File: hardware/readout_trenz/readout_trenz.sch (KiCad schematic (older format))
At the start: 1 part

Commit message: Finishing Readout Schematic
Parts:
- gave numbers to parts that had none: 1
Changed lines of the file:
@@
 B2_[0..31]
 Wire Wire Line
-	12850 5050 12800 5050
-Connection ~ 12850 5050
+	13100 5200 13050 5200
+Connection ~ 13100 5200
 Wire Wire Line
-	12850 5050 12850 5200
+	13100 5200 13100 5350
 Wire Wire Line
-	12800 4950 12850 4950
+	13050 5100 13100 5100
 Wire Wire Line
-	12850 4950 12850 5050
-Text Label 11750 5050 0    50   ~ 0
+	13100 5100 13100 5200
+Text Label 12000 5200 0    50   ~ 0
 LVDS_GPIO_n2
 Wire Wire Line
-	12300 4950 11750 4950
+	12550 5100 12000 5100
 Wire Wire Line
-	11750 5050 12300 5050
+	12000 5200 12550 5200
 $Comp
-L power:GNDD #PWR?
+L power:GNDD #PWR01
 U 1 1 60B06DB5
-P 12850 5200
-F 0 "#PWR?" H 12850 4950 50  0001 C CNN
-F 1 "GNDD-power" H 12854 5045 50  0000 C CNN
-F 2 "" H 12850 5200 50  0001 C CNN
-F 3 "" H 12850 5200 50  0001 C CNN
-	1    12850 5200
+P 13100 5350
+F 0 "#PWR01" H 13100 5100 50  0001 C CNN
+F 1 "GNDD-power" H 13104 5195 50  0000 C CNN
+F 2 "" H 13100 5350 50  0001 C CNN
+F 3 "" H 13100 5350 50  0001 C CNN
+	1    13100 5350
 	1    0    0    -1
 $EndComp
-Connection ~ 12850 4950
+Connection ~ 13100 5100
 $Comp
-L Connector_Generic:Conn_02x12_Counter_Clockwise J?
+L Connector_Generic:Conn_02x12_Counter_Clockwise J1
 U 1 1 60B1DFBC
-P 12500 4450
-F 0 "J?" H 12550 5167 50  0000 C CNN
-F 1 "Conn_02x12_Counter_Clockwise" H 12550 5076 50  0000 C CNN
-F 2 "" H 12500 4450 50  0001 C CNN
-F 3 "~" H 12500 4450 50  0001 C CNN
-	1    12500 4450
+P 12750 4600
+F 0 "J1" H 12800 5317 50  0000 C CNN
+F 1 "Conn_02x12_Counter_Clockwise" H 12800 5226 50  0000 C CNN
+F 2 "" H 12750 4600 50  0001 C CNN
+F 3 "~" H 12750 4600 50  0001 C CNN
+	1    12750 4600
 	1    0    0    -1
 $EndComp
 Wire Wire Line
-	12300 4450 11850 4450
+	12550 4600 12100 4600
 Wire Wire Line
-	11850 4350 12300 4350
-Text Label 11850 4450 0    50   ~ 0
+	12100 4500 12550 4500
+Text Label 12100 4600 0    50   ~ 0
 3v3_GPIO2
-Text Label 11850 4350 0    50   ~ 0
+Text Label 12100 4500 0    50   ~ 0
 3v3_GPIO1
 Wire Wire Line
-	12300 4650 11850 4650
+	12550 4800 12100 4800
 Wire Wire Line
-	11850 4550 12300 4550
-Text Label 11850 4650 0    50   ~ 0
+	12100 4700 12550 4700
+Text Label 12100 4800 0    50   ~ 0
 3v3_GPIO4
-Text Label 11850 4550 0    50   ~ 0
+Text Label 12100 4700 0    50   ~ 0
 3v3_GPIO3
-Text Label 11750 4950 0    50   ~ 0
+Text Label 12000 5100 0    50   ~ 0
 LVDS_GPIO_p2
 Wire Wire Line
-	11750 4850 12300 4850
+	12000 5000 12550 5000
 Wire Wire Line
-	12300 4750 11750 4750
-Text Label 11750 4850 0    50   ~ 0
+	12550 4900 12000 4900
+Text Label 12000 5000 0    50   ~ 0
 LVDS_GPIO_n1
-Text Label 11750 4750 0    50   ~ 0
+Text Label 12000 4900 0    50   ~ 0
 LVDS_GPIO_p1
 Wire Wire Line
-	12300 4050 11850 4050
+	12550 4200 12100 4200
 Wire Wire Line
-	11850 3950 12300 3950
-Text Label 11850 4050 0    50   ~ 0
+	12100 4100 12550 4100
+Text Label 12100 4200 0    50   ~ 0
 1v8_GPIO2
-Text Label 11850 3950 0    50   ~ 0
+Text Label 12100 4100 0    50   ~ 0
 1v8_GPIO1
 Wire Wire Line
-	12300 4250 11850 4250
+	12550 4400 12100 4400
 Wire Wire Line
-	11850 4150 12300 4150
-Text Label 11850 4250 0    50   ~ 0
+	12100 4300 12550 4300
+Text Label 12100 4400 0    50   ~ 0
 1v8_GPIO4
-Text Label 11850 4150 0    50   ~ 0
+Text Label 12100 4300 0    50   ~ 0
 1v8_GPIO3
 Wire Wire Line
-	12850 4050 12850 4150
-Connection ~ 12850 4050
+	13100 4200 13100 4300
+Connection ~ 13100 4200
 Wire Wire Line
-	12850 4050 12800 4050
+	13100 4200 13050 4200
 Wire Wire Line
-	12850 4150 12850 4250
-Connection ~ 12850 4150
+	13100 4300 13100 4400
+Connection ~ 13100 4300
 Wire Wire Line
-	12800 4150 12850 4150
+	13050 4300 13100 4300
 Wire Wire Line
-	12850 4250 12850 4350
-Connection ~ 12850 4250
+	13100 4400 13100 4500
+Connection ~ 13100 4400
 Wire Wire Line
-	12850 4250 12800 4250
-Connection ~ 12850 4350
+	13100 4400 13050 4400
+Connection ~ 13100 4500
 Wire Wire Line
-	12850 3950 12850 4050
+	13100 4100 13100 4200
 Wire Wire Line
-	12800 3950 12850 3950
+	13050 4100 13100 4100
 Wire Wire Line
-	12850 4450 12850 4550
-Connection ~ 12850 4450
+	13100 4600 13100 4700
+Connection ~ 13100 4600
 Wire Wire Line
-	12850 4450 12800 4450
+	13100 4600 13050 4600
 Wire Wire Line
-	12850 4550 12850 4650
-Connection ~ 12850 4550
+	13100 4700 13100 4800
+Connection ~ 13100 4700
 Wire Wire Line
-	12800 4550 12850 4550
+	13050 4700 13100 4700
 Wire Wire Line
-	12850 4650 12850 4750
-Connection ~ 12850 4650
+	13100 4800 13100 4900
+Connection ~ 13100 4800
 Wire Wire Line
-	12850 4650 12800 4650
+	13100 4800 13050 4800
 Wire Wire Line
-	12850 4750 12850 4850
-Connection ~ 12850 4750
+	13100 4900 13100 5000
+Connection ~ 13100 4900
 Wire Wire Line
-	12800 4750 12850 4750
+	13050 4900 13100 4900
 Wire Wire Line
-	12850 4850 12850 4950
-Connection ~ 12850 4850
+	13100 5000 13100 5100
+Connection ~ 13100 5000
 Wire Wire Line
-	12850 4850 12800 4850
+	13100 5000 13050 5000
 Wire Wire Line
-	12850 4350 12850 4450
+	13100 4500 13100 4600
 Wire Wire Line
-	12800 4350 12850 4350
+	13050 4500 13100 4500
 Wire Wire Line
 	2500 6000 3500 6000

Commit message: _
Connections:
- wire segments 52 -> 44
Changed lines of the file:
@@
 	2500 6000 3500 6000
-Wire Bus Line
-	1300 6750 800  6750
-Entry Wire Line
-	1400 6150 1300 6250
-Entry Wire Line
-	1400 6250 1300 6350
-Entry Wire Line
-	1400 6350 1300 6450
-Entry Wire Line
-	1400 6450 1300 6550
-Entry Wire Line
-	800  6950 900  7050
-Entry Wire Line
-	800  7050 900  7150
-Entry Wire Line
-	800  7150 900  7250
-Entry Wire Line
-	800  7250 900  7350
-Wire Wire Line
-	1400 6150 1500 6150
-Wire Wire Line
-	1400 6250 1500 6250
-Wire Wire Line
-	1400 6350 1500 6350
-Wire Wire Line
-	1400 6450 1500 6450
-Wire Wire Line
-	900  7050 1000 7050
-Wire Wire Line
-	900  7150 1000 7150
-Wire Wire Line
-	900  7250 1000 7250
-Wire Wire Line
-	900  7350 1000 7350
 Wire Bus Line
 	4500 1500 5500 1500
@@
 F0 "POWER" 50
 F1 "POWER.sch" 50
-F2 "BIAS1" O L 1000 7050 50
-F3 "BIAS2" O L 1000 7150 50
-F4 "BIAS3" O L 1000 7250 50
-F5 "BIAS4" O L 1000 7350 50
-F6 "ENABLE" I R 6000 7050 50
+F2 "ENABLE" I R 6000 7050 50
+F3 "BIAS[1..4]" O L 1000 7050 50
 $EndSheet
 $Sheet
@@
 F1 "Backplane.sch" 50
 F2 "B2_[0..31]" O R 2500 4500 50
-F3 "BIAS1" I L 1500 6150 50
-F4 "BIAS2" I L 1500 6250 50
-F5 "BIAS4" I L 1500 6450 50
-F6 "OUT" O R 2500 6000 50
-F7 "BIAS3" I L 1500 6350 50
-F8 "B1_[0..31]" O R 2500 1500 50
+F3 "OUT" O R 2500 6000 50
+F4 "B1_[0..31]" O R 2500 1500 50
+F5 "BIAS[1..4]" I L 1500 6450 50
 $EndSheet
 NoConn ~ 3500 3000
@@
 	6050 7050 6000 7050
 Wire Bus Line
-	1300 6250 1300 6750
+	1000 7050 900  7050
 Wire Bus Line
-	800  6750 800  7250
+	900  7050 900  6450
+Wire Bus Line
+	900  6450 1500 6450
 $EndSCHEMATC

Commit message: _
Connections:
- net labels added: Serial_ctrl[0..8]ONE, Serial_ctrl[0..8]TWO
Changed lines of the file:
@@
 F2 "B2_[0..31]" I L 3500 4500 50
 F3 "OUT" I L 3500 6000 50
-F4 "T2_[0..31]" O R 4500 4500 50
+F4 "TRIG_OUT[0..31]" O R 4500 4500 50
 F5 "ADC_IN_TWO[0..3]" I R 4500 6000 50
-F6 "CITIROC_IN_TWO[0..24]" I R 4500 5250 50
+F6 "SH_Ctrl[0..24]" I R 4500 5250 50
+F7 "Serial_ctrl[0..8]" I R 4500 5500 50
 $EndSheet
 $Sheet
@@
 F1 "CITIROC_1.sch" 50
 F2 "B1_[0..31]" I L 3500 1500 50
-F3 "T1_[0..31]" O R 4500 1500 50
+F3 "TRIG_OUT[0..31]" O R 4500 1500 50
 F4 "ADC_IN_ONE[0..3]" I R 4500 3000 50
-F5 "CITIROC_IN_ONE[0..24]" I R 4500 2250 50
+F5 "SH_Ctrl[0..24]" I R 4500 2250 50
 F6 "OUT" I L 3500 3000 50
+F7 "Serial_ctrl[0..8]" I R 4500 2500 50
 $EndSheet
 Text Label 2550 1500 0    50   ~ 0
@@
 F0 "Trenz_Module" 79
 F1 "Trenz_Module.sch" 79
-F2 "T1_[0..31]" I L 5500 1500 50
-F3 "T2_[0..31]" I L 5500 4500 50
+F2 "TRIG_OUT[0..31]" I L 5500 1500 50
+F3 "TRIG_OUT[0..31]" I L 5500 4500 50
 F4 "ADC_IN_ONE[0..3]" O L 5500 3000 50
 F5 "ADC_IN_TWO[0..3]" O L 5500 6000 50
-F6 "CITIROC_IN_ONE[0..24]" O L 5500 2250 50
-F7 "CITIROC_IN_TWO[0..24]" O L 5500 5250 50
+F6 "SH_Ctrl[0..24]" O L 5500 2250 50
+F7 "SH_Ctrl[0..24]" O L 5500 5250 50
 F8 "CLOCK" I R 7500 1450 50
 F9 "TRIGGER" I R 7500 1550 50
 F10 "ENABLE" O L 5500 6450 50
+F11 "Serial_ctrl[0..8]" O L 5500 2500 50
+F12 "Serial_ctrl[0..8]" O L 5500 5500 50
 $EndSheet
 Wire Wire Line
@@
 Wire Bus Line
 	900  6450 1500 6450
+Wire Bus Line
+	5500 2500 4500 2500
+Text Label 4600 2500 0    50   ~ 0
+Serial_ctrl[0..8]ONE
+Wire Bus Line
+	4500 5500 5500 5500
+Text Label 4650 5500 0    50   ~ 0
+Serial_ctrl[0..8]TWO
 $EndSCHEMATC

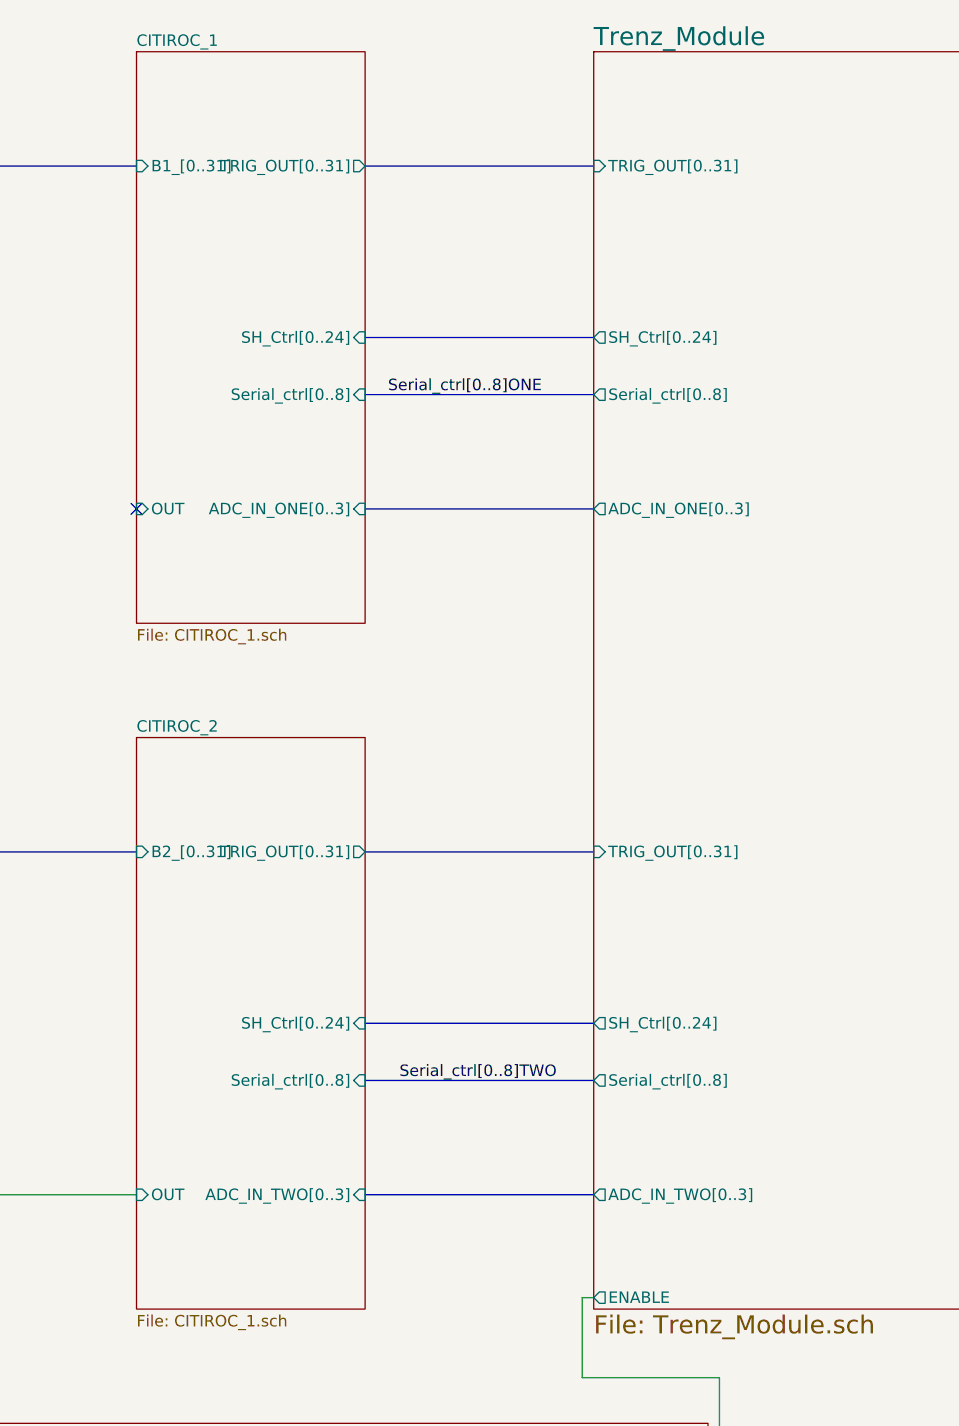
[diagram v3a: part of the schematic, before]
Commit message: Readout Preliminary Schematic Made
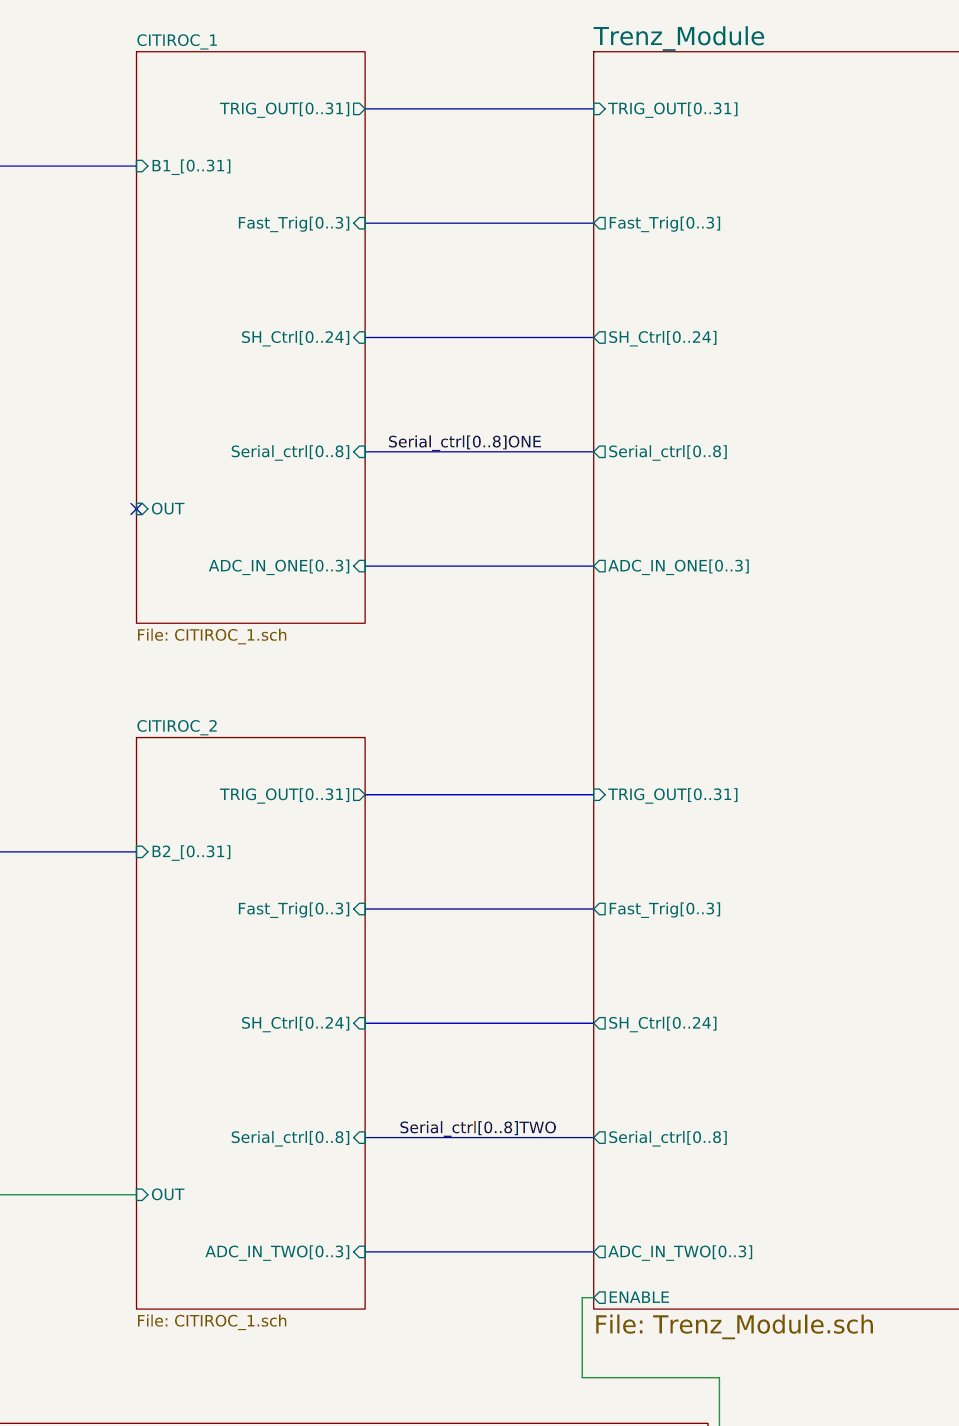
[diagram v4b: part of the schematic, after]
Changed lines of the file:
@@
 	2500 6000 3500 6000
 Wire Bus Line
-	4500 1500 5500 1500
+	4500 1250 5500 1250
 Wire Bus Line
-	4500 4500 5500 4500
+	4500 4250 5500 4250
 Wire Bus Line
-	4500 6000 5500 6000
+	4500 6250 5500 6250
 Wire Bus Line
-	4500 3000 5500 3000
+	4500 3250 5500 3250
 Wire Bus Line
 	4500 2250 5500 2250
@@
 F2 "B2_[0..31]" I L 3500 4500 50
 F3 "OUT" I L 3500 6000 50
-F4 "TRIG_OUT[0..31]" O R 4500 4500 50
-F5 "ADC_IN_TWO[0..3]" I R 4500 6000 50
+F4 "TRIG_OUT[0..31]" O R 4500 4250 50
+F5 "ADC_IN_TWO[0..3]" I R 4500 6250 50
 F6 "SH_Ctrl[0..24]" I R 4500 5250 50
-F7 "Serial_ctrl[0..8]" I R 4500 5500 50
-$EndSheet
-$Sheet
-S 3500 1000 1000 2500
-U 60BB4A14
-F0 "CITIROC_1" 50
-F1 "CITIROC_1.sch" 50
-F2 "B1_[0..31]" I L 3500 1500 50
-F3 "TRIG_OUT[0..31]" O R 4500 1500 50
-F4 "ADC_IN_ONE[0..3]" I R 4500 3000 50
-F5 "SH_Ctrl[0..24]" I R 4500 2250 50
-F6 "OUT" I L 3500 3000 50
-F7 "Serial_ctrl[0..8]" I R 4500 2500 50
+F7 "Serial_ctrl[0..8]" I R 4500 5750 50
+F8 "Fast_Trig[0..3]" I R 4500 4750 50
 $EndSheet
 Text Label 2550 1500 0    50   ~ 0
@@
 F0 "Trenz_Module" 79
 F1 "Trenz_Module.sch" 79
-F2 "TRIG_OUT[0..31]" I L 5500 1500 50
-F3 "TRIG_OUT[0..31]" I L 5500 4500 50
-F4 "ADC_IN_ONE[0..3]" O L 5500 3000 50
-F5 "ADC_IN_TWO[0..3]" O L 5500 6000 50
+F2 "TRIG_OUT[0..31]" I L 5500 1250 50
+F3 "TRIG_OUT[0..31]" I L 5500 4250 50
+F4 "ADC_IN_ONE[0..3]" O L 5500 3250 50
+F5 "ADC_IN_TWO[0..3]" O L 5500 6250 50
 F6 "SH_Ctrl[0..24]" O L 5500 2250 50
 F7 "SH_Ctrl[0..24]" O L 5500 5250 50
@@
 F9 "TRIGGER" I R 7500 1550 50
 F10 "ENABLE" O L 5500 6450 50
-F11 "Serial_ctrl[0..8]" O L 5500 2500 50
-F12 "Serial_ctrl[0..8]" O L 5500 5500 50
+F11 "Serial_ctrl[0..8]" O L 5500 2750 50
+F12 "Serial_ctrl[0..8]" O L 5500 5750 50
+F13 "Fast_Trig[0..3]" O L 5500 1750 50
+F14 "Fast_Trig[0..3]" O L 5500 4750 50
 $EndSheet
 Wire Wire Line
@@
 	900  6450 1500 6450
 Wire Bus Line
-	5500 2500 4500 2500
-Text Label 4600 2500 0    50   ~ 0
+	5500 2750 4500 2750
+Text Label 4600 2750 0    50   ~ 0
 Serial_ctrl[0..8]ONE
 Wire Bus Line
-	4500 5500 5500 5500
-Text Label 4650 5500 0    50   ~ 0
+	4500 5750 5500 5750
+Text Label 4650 5750 0    50   ~ 0
 Serial_ctrl[0..8]TWO
+$Sheet
+S 3500 1000 1000 2500
+U 60BB4A14
+F0 "CITIROC_1" 50
+F1 "CITIROC_1.sch" 50
+F2 "B1_[0..31]" I L 3500 1500 50
+F3 "TRIG_OUT[0..31]" O R 4500 1250 50
+F4 "ADC_IN_ONE[0..3]" I R 4500 3250 50
+F5 "SH_Ctrl[0..24]" I R 4500 2250 50
+F6 "OUT" I L 3500 3000 50
+F7 "Serial_ctrl[0..8]" I R 4500 2750 50
+F8 "Fast_Trig[0..3]" I R 4500 1750 50
+$EndSheet
+Wire Bus Line
+	5500 1750 4500 1750
+Wire Bus Line
+	5500 4750 4500 4750
 $EndSCHEMATC

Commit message: Footprints Assigned
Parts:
- removed J1: Conn_02x12_Counter_Clockwise, symbol Connector_Generic:Conn_02x12_Counter_Clockwise
- added J1: Conn_02x05_Odd_Even, Connector_PinHeader_2.54mm:PinHeader_2x05_P2.54mm_Vertical_SMD, symbol Connector_Generic:Conn_02x05_Odd_Even
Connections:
- net labels added: GNDD, UNUSED0, UNUSED1, UNUSED2, UNUSED3, UNUSED4
- net labels removed: GNDD-power
- wire segments 44 -> 35
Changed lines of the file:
@@
 Text Label 2550 4500 0    50   ~ 0
 B2_[0..31]
-Wire Wire Line
-	13100 5200 13050 5200
-Connection ~ 13100 5200
-Wire Wire Line
-	13100 5200 13100 5350
-Wire Wire Line
-	13050 5100 13100 5100
-Wire Wire Line
-	13100 5100 13100 5200
-Text Label 12000 5200 0    50   ~ 0
+Text Label 11550 5250 0    50   ~ 0
 LVDS_GPIO_n2
 Wire Wire Line
-	12550 5100 12000 5100
-Wire Wire Line
-	12000 5200 12550 5200
-$Comp
-L power:GNDD #PWR01
-U 1 1 60B06DB5
-P 13100 5350
-F 0 "#PWR01" H 13100 5100 50  0001 C CNN
-F 1 "GNDD-power" H 13104 5195 50  0000 C CNN
-F 2 "" H 13100 5350 50  0001 C CNN
-F 3 "" H 13100 5350 50  0001 C CNN
-	1    13100 5350
-	1    0    0    -1
-$EndComp
-Connection ~ 13100 5100
-$Comp
-L Connector_Generic:Conn_02x12_Counter_Clockwise J1
-U 1 1 60B1DFBC
-P 12750 4600
-F 0 "J1" H 12800 5317 50  0000 C CNN
-F 1 "Conn_02x12_Counter_Clockwise" H 12800 5226 50  0000 C CNN
-F 2 "" H 12750 4600 50  0001 C CNN
-F 3 "~" H 12750 4600 50  0001 C CNN
-	1    12750 4600
-	1    0    0    -1
-$EndComp
-Wire Wire Line
-	12550 4600 12100 4600
-Wire Wire Line
-	12100 4500 12550 4500
-Text Label 12100 4600 0    50   ~ 0
+	12100 5150 11550 5150
+Wire Wire Line
+	11550 5250 12100 5250
+Wire Wire Line
+	12100 4650 11650 4650
+Wire Wire Line
+	11650 4550 12100 4550
+Text Label 11650 4650 0    50   ~ 0
 3v3_GPIO2
-Text Label 12100 4500 0    50   ~ 0
+Text Label 11650 4550 0    50   ~ 0
 3v3_GPIO1
 Wire Wire Line
-	12550 4800 12100 4800
-Wire Wire Line
-	12100 4700 12550 4700
-Text Label 12100 4800 0    50   ~ 0
+	12100 4850 11650 4850
+Wire Wire Line
+	11650 4750 12100 4750
+Text Label 11650 4850 0    50   ~ 0
 3v3_GPIO4
-Text Label 12100 4700 0    50   ~ 0
+Text Label 11650 4750 0    50   ~ 0
 3v3_GPIO3
-Text Label 12000 5100 0    50   ~ 0
+Text Label 11550 5150 0    50   ~ 0
 LVDS_GPIO_p2
 Wire Wire Line
-	12000 5000 12550 5000
-Wire Wire Line
-	12550 4900 12000 4900
-Text Label 12000 5000 0    50   ~ 0
+	11550 5050 12100 5050
+Wire Wire Line
+	12100 4950 11550 4950
+Text Label 11550 5050 0    50   ~ 0
 LVDS_GPIO_n1
-Text Label 12000 4900 0    50   ~ 0
+Text Label 11550 4950 0    50   ~ 0
 LVDS_GPIO_p1
 Wire Wire Line
-	12550 4200 12100 4200
-Wire Wire Line
-	12100 4100 12550 4100
-Text Label 12100 4200 0    50   ~ 0
+	12100 4250 11650 4250
+Wire Wire Line
+	11650 4150 12100 4150
+Text Label 11650 4250 0    50   ~ 0
 1v8_GPIO2
-Text Label 12100 4100 0    50   ~ 0
+Text Label 11650 4150 0    50   ~ 0
 1v8_GPIO1
 Wire Wire Line
-	12550 4400 12100 4400
-Wire Wire Line
-	12100 4300 12550 4300
-Text Label 12100 4400 0    50   ~ 0
+	12100 4450 11650 4450
+Wire Wire Line
+	11650 4350 12100 4350
+Text Label 11650 4450 0    50   ~ 0
 1v8_GPIO4
-Text Label 12100 4300 0    50   ~ 0
+Text Label 11650 4350 0    50   ~ 0
 1v8_GPIO3
-Wire Wire Line
-	13100 4200 13100 4300
-Connection ~ 13100 4200
-Wire Wire Line
-	13100 4200 13050 4200
-Wire Wire Line
-	13100 4300 13100 4400
-Connection ~ 13100 4300
-Wire Wire Line
-	13050 4300 13100 4300
-Wire Wire Line
-	13100 4400 13100 4500
-Connection ~ 13100 4400
-Wire Wire Line
-	13100 4400 13050 4400
-Connection ~ 13100 4500
-Wire Wire Line
-	13100 4100 13100 4200
-Wire Wire Line
-	13050 4100 13100 4100
-Wire Wire Line
-	13100 4600 13100 4700
-Connection ~ 13100 4600
-Wire Wire Line
-	13100 4600 13050 4600
-Wire Wire Line
-	13100 4700 13100 4800
-Connection ~ 13100 4700
-Wire Wire Line
-	13050 4700 13100 4700
-Wire Wire Line
-	13100 4800 13100 4900
-Connection ~ 13100 4800
-Wire Wire Line
-	13100 4800 13050 4800
-Wire Wire Line
-	13100 4900 13100 5000
-Connection ~ 13100 4900
-Wire Wire Line
-	13050 4900 13100 4900
-Wire Wire Line
-	13100 5000 13100 5100
-Connection ~ 13100 5000
-Wire Wire Line
-	13100 5000 13050 5000
-Wire Wire Line
-	13100 4500 13100 4600
-Wire Wire Line
-	13050 4500 13100 4500
 Wire Wire Line
 	2500 6000 3500 6000
@@
 F13 "Fast_Trig[0..3]" O L 5500 1750 50
 F14 "Fast_Trig[0..3]" O L 5500 4750 50
+F15 "UNUSED[0..4]" B R 7500 3250 50
 $EndSheet
 Wire Wire Line
@@
 Wire Bus Line
 	5500 4750 4500 4750
+$Comp
+L Connector_Generic:Conn_02x05_Odd_Even J1
+U 1 1 60DDF7C6
+P 8700 3750
+F 0 "J1" H 8750 4167 50  0000 C CNN
+F 1 "Conn_02x05_Odd_Even" H 8750 4076 50  0000 C CNN
+F 2 "Connector_PinHeader_2.54mm:PinHeader_2x05_P2.54mm_Vertical_SMD" H 8700 3750 50  0001 C CNN
+F 3 "~" H 8700 3750 50  0001 C CNN
+	1    8700 3750
+	1    0    0    -1
+$EndComp
+Wire Wire Line
+	9000 3550 9100 3550
+Wire Wire Line
+	9100 3550 9100 3650
+Wire Wire Line
+	9000 3650 9100 3650
+Connection ~ 9100 3650
+Wire Wire Line
+	9100 3650 9100 3750
+Wire Wire Line
+	9000 3750 9100 3750
+Connection ~ 9100 3750
+Wire Wire Line
+	9100 3750 9100 3850
+Wire Wire Line
+	9000 3850 9100 3850
+Connection ~ 9100 3850
+Wire Wire Line
+	9100 3850 9100 3950
+Wire Wire Line
+	9000 3950 9100 3950
+Connection ~ 9100 3950
+Wire Wire Line
+	9100 3950 9100 4050
+$Comp
+L power:GNDD #PWR01
+U 1 1 60DE3614
+P 9100 4050
+F 0 "#PWR01" H 9100 3800 50  0001 C CNN
+F 1 "GNDD" H 9104 3895 50  0000 C CNN
+F 2 "" H 9100 4050 50  0001 C CNN
+F 3 "" H 9100 4050 50  0001 C CNN
+	1    9100 4050
+	1    0    0    -1
+$EndComp
+Text Label 8000 3550 0    50   ~ 0
+UNUSED0
+Text Label 8000 3650 0    50   ~ 0
+UNUSED1
+Text Label 8000 3750 0    50   ~ 0
+UNUSED2
+Text Label 8000 3850 0    50   ~ 0
+UNUSED3
+Text Label 8000 3950 0    50   ~ 0
+UNUSED4
+Wire Wire Line
+	8500 3550 8000 3550
+Wire Wire Line
+	8500 3650 8000 3650
+Wire Wire Line
+	8500 3750 8000 3750
+Wire Wire Line
+	8500 3850 8000 3850
+Wire Wire Line
+	8500 3950 8000 3950
+Entry Wire Line
+	7900 3450 8000 3550
+Entry Wire Line
+	7900 3550 8000 3650
+Entry Wire Line
+	7900 3650 8000 3750
+Entry Wire Line
+	7900 3750 8000 3850
+Entry Wire Line
+	7900 3850 8000 3950
+Wire Bus Line
+	7900 3250 7500 3250
+Wire Bus Line
+	7900 3250 7900 3850
 $EndSCHEMATC
